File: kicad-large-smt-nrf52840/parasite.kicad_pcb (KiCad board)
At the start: 4 copper layers, 22 x 126.4 mm, 55 parts, among them J1 TC2030-SWD, Q1 MMBT3906, Q4 Q_Photo_NPN, SW1 B3U-1000P, U1 nRF52840-QIAA, U2 SHTC3, Y1 32.768kHz, Y2 32MHz

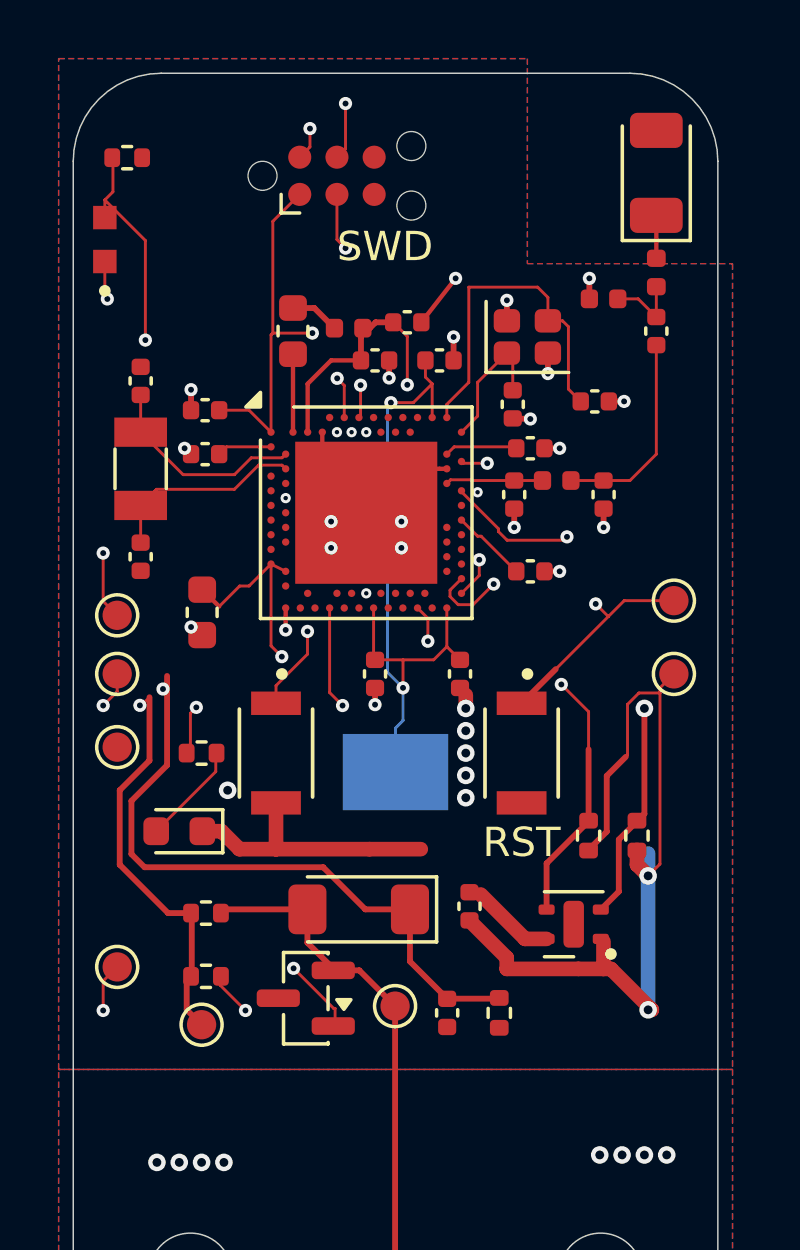
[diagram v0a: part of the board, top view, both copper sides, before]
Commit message: feat: enlarge ordinary passives and document approved package exceptions
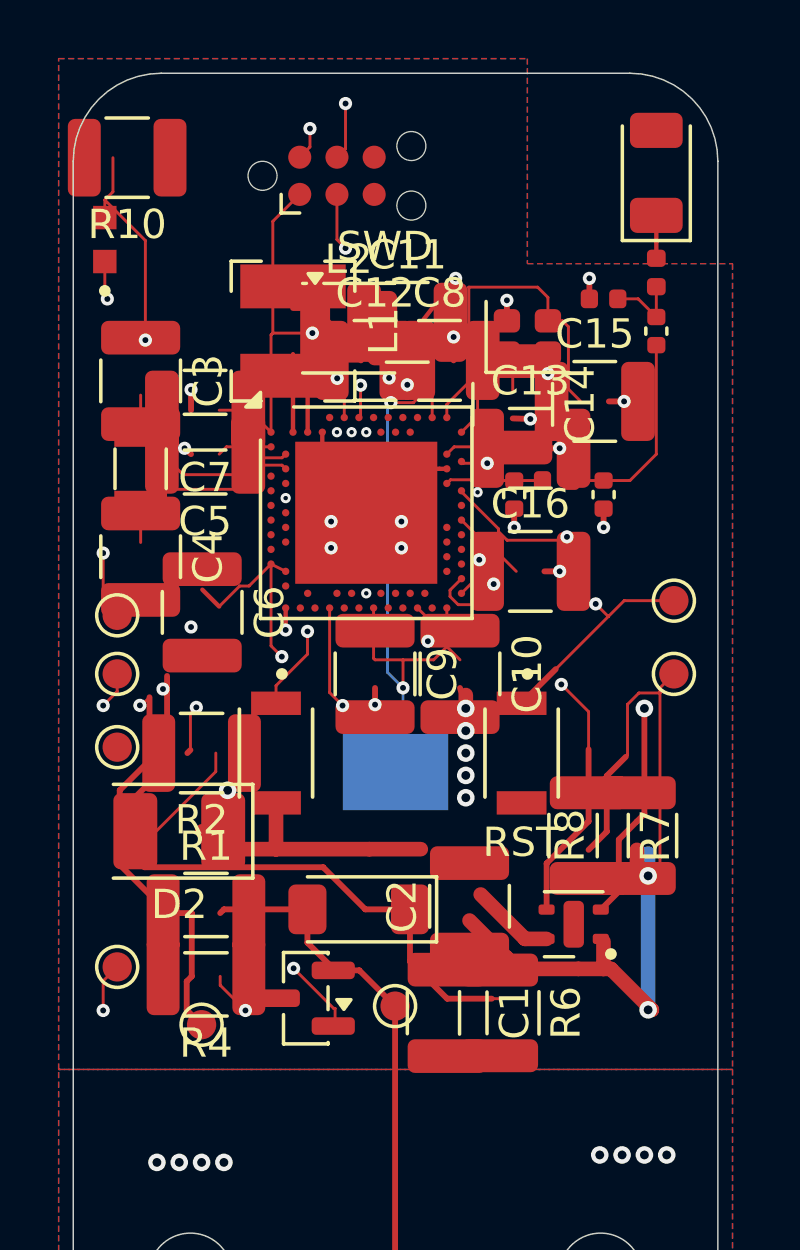
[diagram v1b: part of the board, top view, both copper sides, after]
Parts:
- C1, C10, C11, C12, C13, C14, C15, C16, C2, C3, C4, C5, C7, C8, C9: footprint Capacitor_SMD:C_0402_1005Metric -> Capacitor_SMD:C_1210_3225Metric
- C6: footprint Capacitor_SMD:C_0603_1608Metric -> Capacitor_SMD:C_1210_3225Metric
- D2: footprint LED_SMD:LED_0603_1608Metric -> LED_SMD:LED_PLCC-2_3.4x3.0mm_KA
- L1: footprint Inductor_SMD:L_0603_1608Metric -> Inductor_SMD:L_Bourns-SRN4018
- L2: footprint Inductor_SMD:L_0402_1005Metric -> Inductor_SMD:L_Coilcraft_1008HQ_2520Metric
- R1, R10, R2, R4, R6, R7, R8: footprint Resistor_SMD:R_0402_1005Metric -> Resistor_SMD:R_1210_3225Metric
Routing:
- net Net-(D2-A): vias 0 -> 1
- net GND: vias 36 -> 35

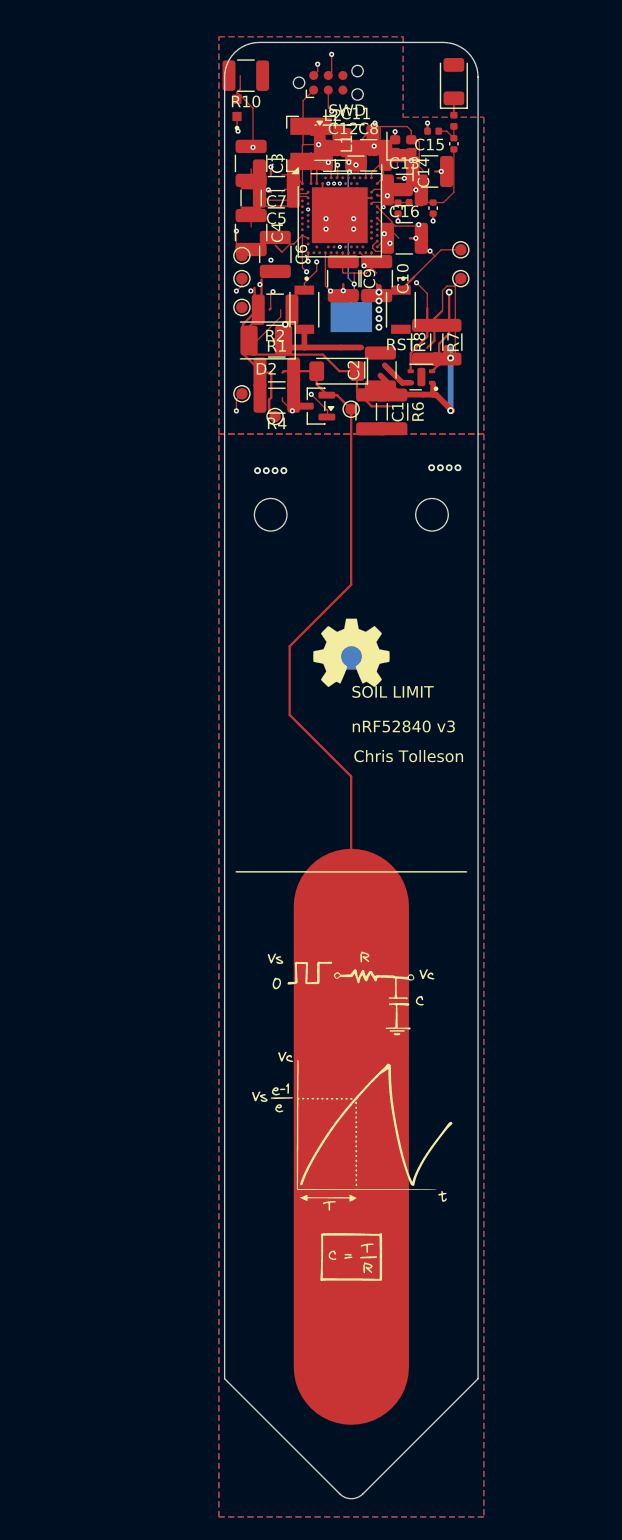
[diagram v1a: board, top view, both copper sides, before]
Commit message: checkpoint: preserve unfinished large-SMT layout before module selection
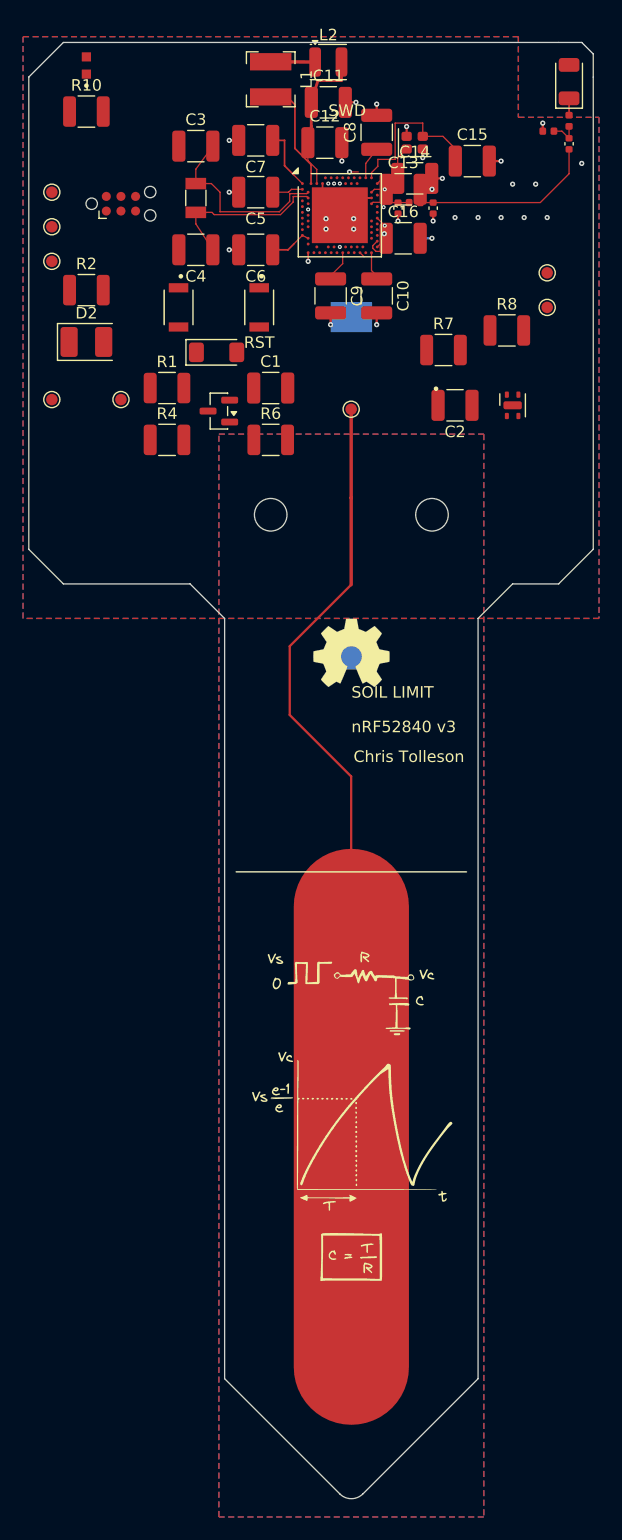
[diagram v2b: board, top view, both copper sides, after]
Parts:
- moved J1 20.8 mm to (48.0, 41.0)
- moved TP1 17.4 mm to (42.0, 40.0)
- moved TP2 17.1 mm to (42.0, 43.0)
- moved TP3 17.0 mm to (42.0, 46.0)
- moved TP8 16.5 mm to (42.0, 58.0)
- moved R2 16.5 mm to (45.0, 48.5), turned to 0 degrees
- moved D2 15.6 mm to (45.0, 53.0), turned to 0 degrees
- moved R10 14.2 mm to (45.0, 33.0), turned to 0 degrees
- moved Q4 13.6 mm to (45.0, 29.0)
- moved TP6 13.5 mm to (48.0, 58.0)
- moved RST1 12.3 mm to (60.0, 50.0)
- moved SW1 10.9 mm to (53.0, 50.0)
- moved R6 10.8 mm to (61.0, 61.5), turned to 0 degrees
- moved D1 10.6 mm to (56.3, 53.9), turned to 0 degrees
- moved R4 10.2 mm to (52.0, 61.5), turned to 0 degrees
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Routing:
- net +3V0: track 95.4 -> 18.1 mm, vias 6 -> 1
- net SWDCLK: track 47.6 -> 1.67 mm, vias 3 -> 0
- net 0.10: track 40.6 -> 0.04 mm, vias 2 -> 0
- net SENS_OUT: track 36.2 -> 1.61 mm, vias 2 -> 1
- net SWDIO: track 39.3 -> 10.4 mm, vias 3 -> 1
- net RST: track 32.2 -> 3.39 mm, vias 3 -> 1
- net PWM: track 24.9 -> 0.00 mm, vias 2 -> 1
- net SCL: track 25.1 -> 0.35 mm, vias 2 -> 0
- net PHOTO_OUT: track 16.8 -> 0.08 mm, vias 2 -> 0
- net SDA: track 15.1 -> 0.50 mm, vias 2 -> 0
- net LED: track 14.3 -> 0.87 mm, vias 2 -> 1
- net PHOTO_V: track 11.7 -> 0.00 mm, vias 2 -> 0
- net XL1: track 7.11 -> 16.6 mm
- net BTN1: track 10.6 -> 1.42 mm, vias 2 -> 1
- net RF_50: track 7.01 -> 16.1 mm
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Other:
- board size 22 x 126.4 mm -> 49 x 126.4 mm
